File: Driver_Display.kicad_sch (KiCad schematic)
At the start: 0 parts

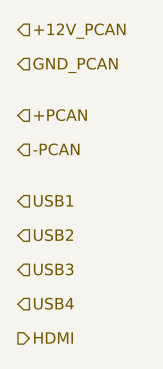
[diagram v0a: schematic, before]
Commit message: Updated Controls + Telemetry
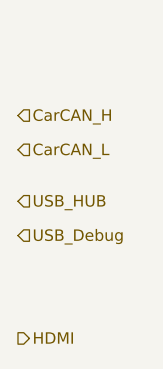
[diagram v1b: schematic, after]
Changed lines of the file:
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@@
 	(generator_version "9.0")
 	(paper "A4")
-	(hierarchical_label "USB3"
-		(shape input)
-		(at 143.51 114.3 0)
-		(effects
-			(font
-				(size 1.27 1.27)
-			)
-			(justify left)
-		)
-	)
-	(hierarchical_label "-PCAN"
+	(hierarchical_label "CarCAN_L"
 		(shape input)
 		(at 143.51 100.965 0)
@@
 		)
 	)
-	(hierarchical_label "GND_PCAN"
+	(hierarchical_label "USB_Debug"
 		(shape input)
-		(at 143.51 91.44 0)
+		(at 143.51 110.49 0)
 		(effects
 			(font
@@
 		)
 	)
-	(hierarchical_label "USB4"
-		(shape input)
-		(at 143.51 118.11 0)
-		(effects
-			(font
-				(size 1.27 1.27)
-			)
-			(justify left)
-		)
-	)
-	(hierarchical_label "+PCAN"
+	(hierarchical_label "CarCAN_H"
 		(shape input)
 		(at 143.51 97.155 0)
@@
 		)
 	)
-	(hierarchical_label "USB1"
+	(hierarchical_label "USB_HUB"
 		(shape input)
 		(at 143.51 106.68 0)
-		(effects
-			(font
-				(size 1.27 1.27)
-			)
-			(justify left)
-		)
-	)
-	(hierarchical_label "+12V_PCAN"
-		(shape input)
-		(at 143.51 87.63 0)
 		(effects
 			(font
@@
 		(effects
 			(font
-				(size 1.27 1.27)
-			)
-			(justify left)
-		)
-	)
-	(hierarchical_label "USB2"
-		(shape input)
-		(at 143.51 110.49 0)
-		(effects
-			(font
